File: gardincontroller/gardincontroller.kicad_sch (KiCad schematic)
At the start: 23 parts, among them J1 Conn_01x04_Male, J2 USB_C_Receptacle_USB2.0, U1 ESP32-S2-MINI-1-N4, U2 LM1117-3.3

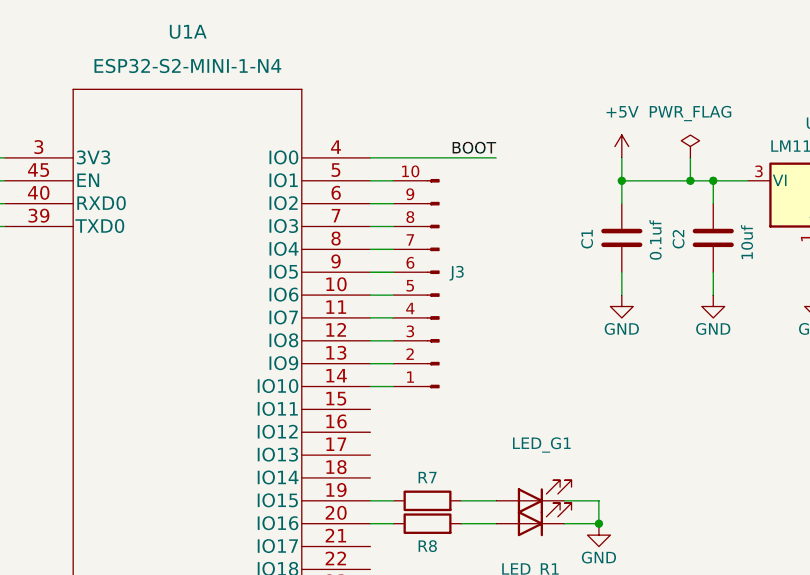
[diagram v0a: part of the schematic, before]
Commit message: 11 pin header istedet
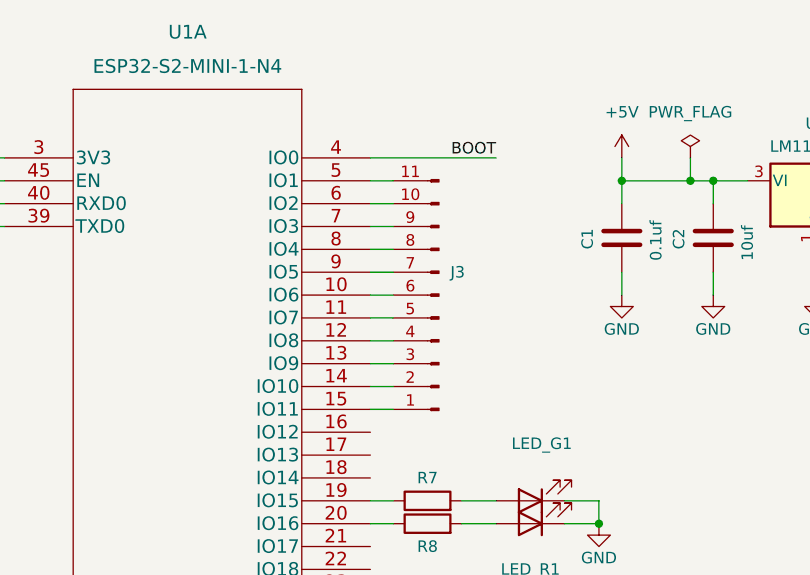
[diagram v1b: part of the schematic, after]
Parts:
- J3: symbol Connector:Conn_01x10_Male -> Connector:Conn_01x11_Male
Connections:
- net at J3.1 (Pin_1): now also U1.15 (IO11); no longer U1.14 (IO10)
- net at J3.10 (Pin_10): now also U1.6 (IO2); no longer U1.5 (IO1)
- net at J3.2 (Pin_2): now also U1.14 (IO10); no longer U1.13 (IO9)
- net at J3.3 (Pin_3): now also U1.13 (IO9); no longer U1.12 (IO8)
- net at J3.4 (Pin_4): now also U1.12 (IO8); no longer U1.11 (IO7)
- net at J3.5 (Pin_5): now also U1.11 (IO7); no longer U1.10 (IO6)
- net at J3.6 (Pin_6): now also U1.10 (IO6); no longer U1.9 (IO5)
- net at J3.7 (Pin_7): now also U1.9 (IO5); no longer U1.8 (IO4)
- net at J3.8 (Pin_8): now also U1.8 (IO4); no longer U1.7 (IO3)
- net at J3.9 (Pin_9): now also U1.7 (IO3); no longer U1.6 (IO2)
- new net: J3.11 (Pin_11), U1.5 (IO1)
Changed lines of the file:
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@@
+    (stroke (width 0) (type default) (color 0 0 0 0))
+  )
+  (wire (pts (xy 137.16 80.01) (xy 139.7 80.01))
     (stroke (width 0) (type default) (color 0 0 0 0))
   )
@@
     (pin "2")
   )
-  (symbol (lib_id "Connector:Conn_01x10_Male") (at 144.78 67.31 180) (unit 1)
+  (symbol (lib_id "Connector:Conn_01x11_Male") (at 144.78 67.31 180) (unit 1)
     (in_bom yes) (on_board yes) (fields_autoplaced)
     (property "Reference" "J3" (id 0) (at 146.05 64.7699 0)
@@
     (pin "1")
     (pin "10")
+    (pin "11")
     (pin "2")
     (pin "3")
@@
     )
     (path "/1659721a-2aef-4367-b25a-0fc52655fc3e"
-      (reference "J3") (unit 1) (value "Conn_01x10_Male") (footprint "Connector_PinHeader_2.54mm:PinHeader_1x10_P2.54mm_Vertical")
+      (reference "J3") (unit 1) (value "Conn_01x10_Male") (footprint "Connector_PinHeader_2.54mm:PinHeader_1x11_P2.54mm_Vertical")
     )
     (path "/1d026b84-5f07-4dc1-b1f4-e6503fe2e69e"
